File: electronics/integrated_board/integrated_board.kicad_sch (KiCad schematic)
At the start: 69 parts, among them CON1 BARREL_JACK, J1 rot_encoderZ(35,34), J10 pcf8575 IO expander, J11 Switch 1, J13 motor1(15,2,0,4), J15 motor2 (16,17,5,18), J17 motor3 (19,21,22,23), J2 rot_encoderY(25,26), J3 rot_encoderX(14,27), J4 Switch 2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

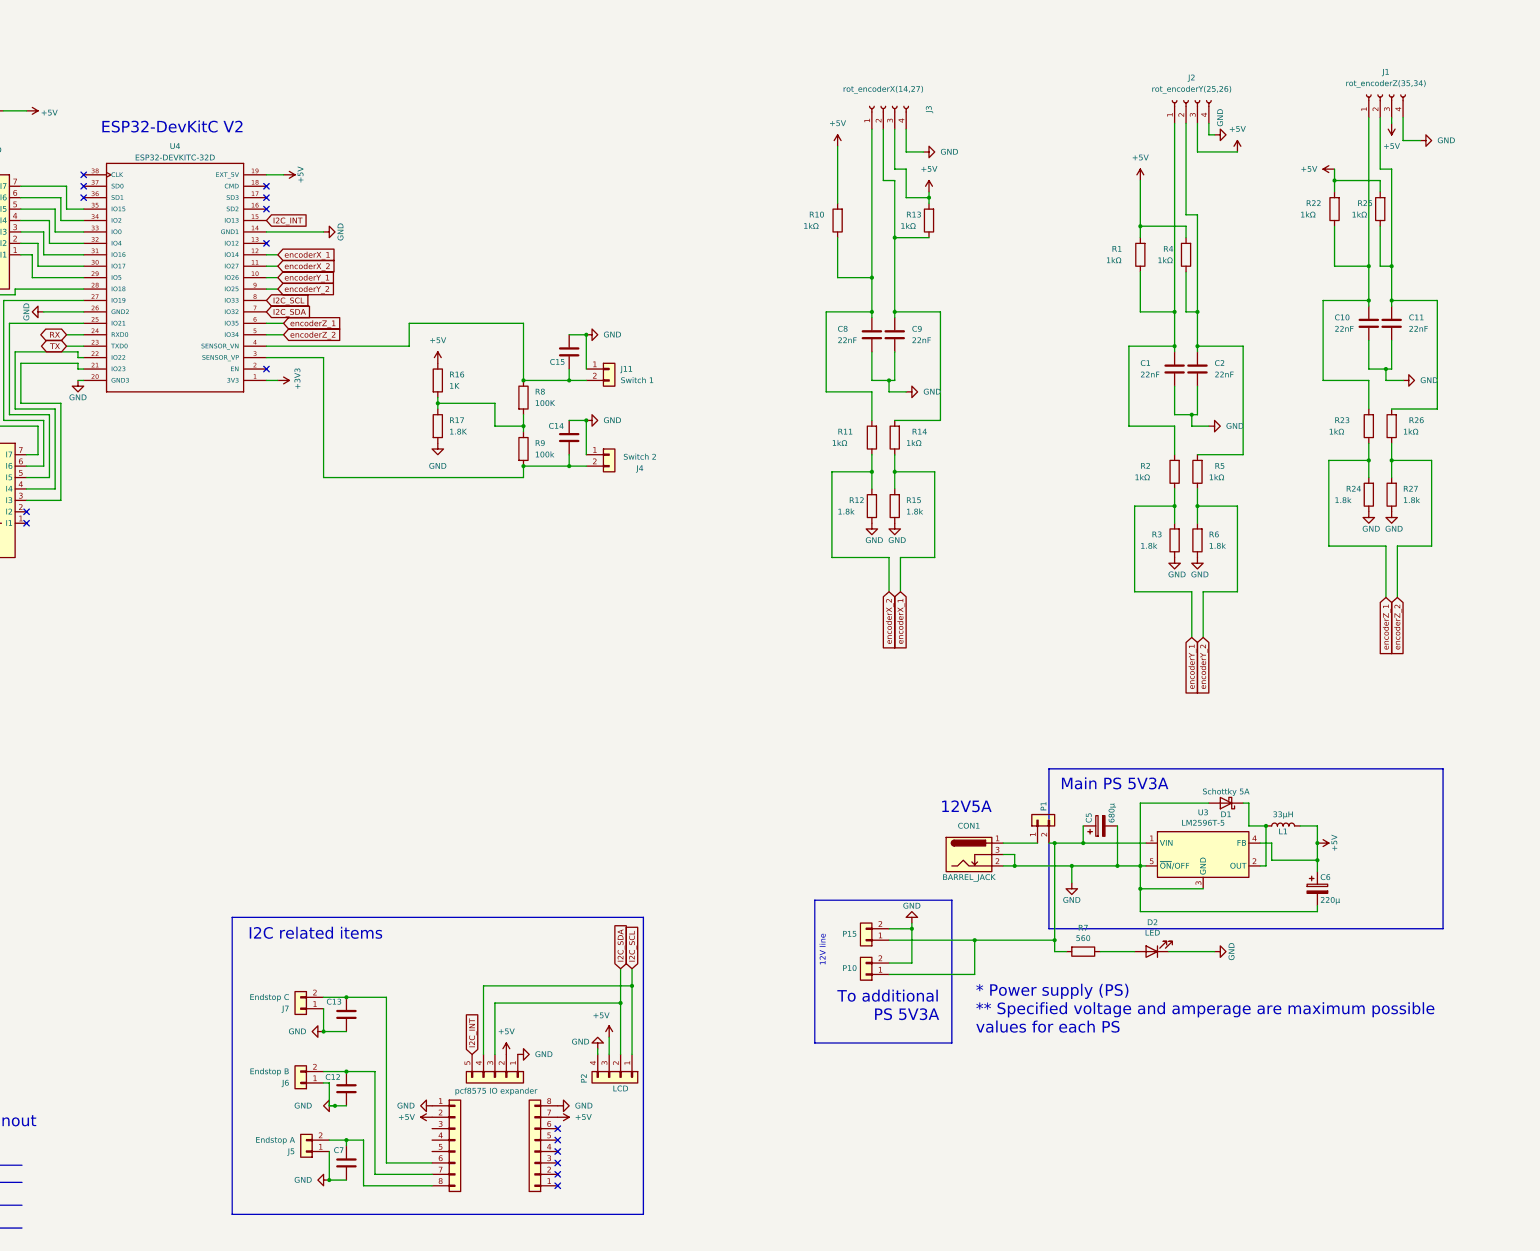
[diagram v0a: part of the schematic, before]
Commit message: Updated integrated PCB
- fixed footprint for pcf8575
- updated footprint for rotary encoder connectors for ease of use
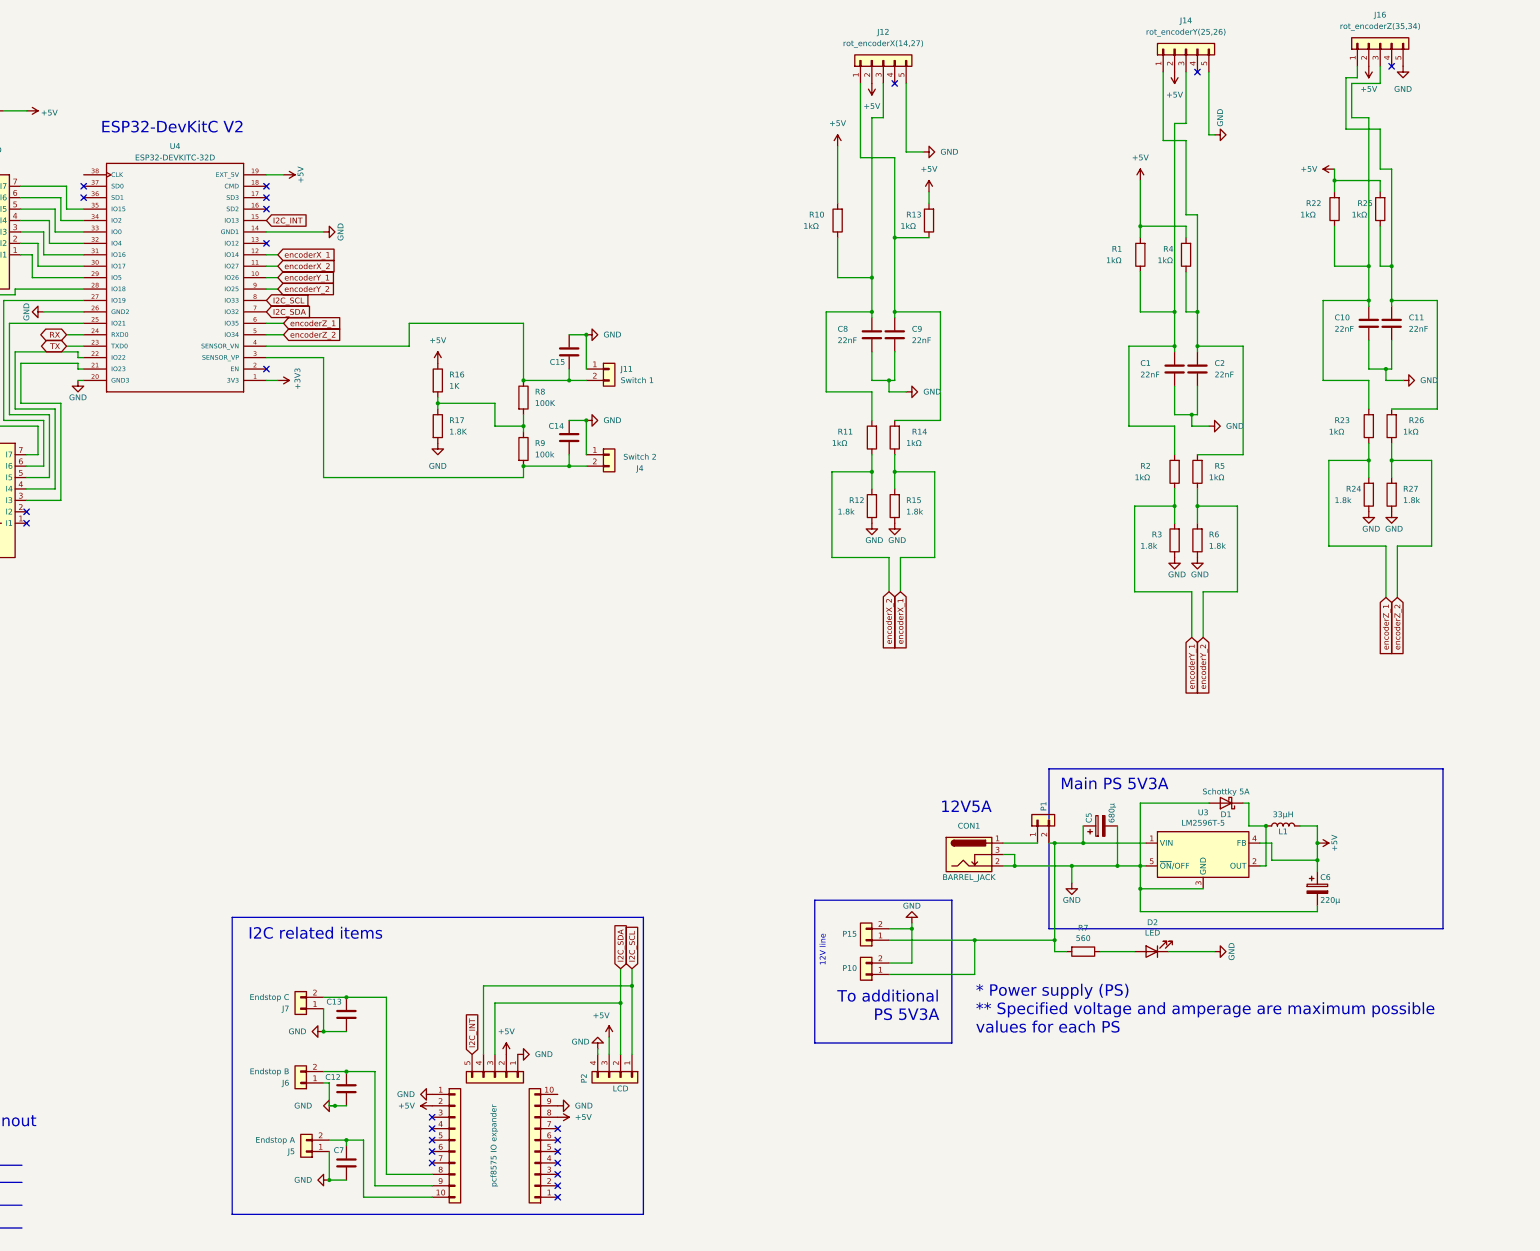
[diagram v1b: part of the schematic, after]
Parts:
- removed J1: rot_encoderZ(35,34), Connector_JST:JST_XH_B4B-XH-A_1x04_P2.50mm_Vertical, symbol Connector:Conn_01x04_Female
- removed J2: rot_encoderY(25,26), Connector_JST:JST_XH_B4B-XH-A_1x04_P2.50mm_Vertical, symbol Connector:Conn_01x04_Female
- removed J3: rot_encoderX(14,27), Connector_JST:JST_XH_B4B-XH-A_1x04_P2.50mm_Vertical, symbol Connector:Conn_01x04_Female
- added J12: rot_encoderX(14,27), Connector_JST:JST_XH_B5B-XH-A_1x05_P2.50mm_Vertical, symbol Connector_Generic:Conn_01x05
- added J14: rot_encoderY(25,26), Connector_JST:JST_XH_B5B-XH-A_1x05_P2.50mm_Vertical, symbol Connector_Generic:Conn_01x05
- added J16: rot_encoderZ(35,34), Connector_JST:JST_XH_B5B-XH-A_1x05_P2.50mm_Vertical, symbol Connector_Generic:Conn_01x05
- J8, J9: footprint Connector_PinHeader_2.54mm:PinHeader_1x08_P2.54mm_Vertical -> Connector_PinHeader_2.54mm:PinHeader_1x10_P2.54mm_Vertical; symbol Connector_Generic:Conn_01x08 -> Connector_Generic:Conn_01x10
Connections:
- net +5V: now also J8.8 (Pin_8), J12.2 (Pin_2), J14.2 (Pin_2), J16.2 (Pin_2); no longer J8.7 (Pin_7)
- net GND: now also J8.9 (Pin_9), J12.5 (Pin_5), J14.5 (Pin_5), J16.5 (Pin_5); no longer J8.8 (Pin_8)
- net at C10.2, R22.1, R23.2: now also J16.3 (Pin_3)
- net at C11.2, R25.1, R26.2: now also J16.1 (Pin_1)
- net at C8.2, R10.1, R11.2: now also J12.3 (Pin_3)
- net at C2.2, R4.1, R5.2: now also J14.1 (Pin_1)
- net at C9.2, R13.1, R14.2: now also J12.1 (Pin_1)
- net at C7.2, J5.2 (Pin_2): now also J9.10 (Pin_10); no longer J9.8 (Pin_8)
- net at C1.2, R1.1, R2.2: now also J14.3 (Pin_3)
- net at C12.2, J6.2 (Pin_2): now also J9.9 (Pin_9); no longer J9.7 (Pin_7)
- net at C13.2, J7.2 (Pin_2): now also J9.8 (Pin_8); no longer J9.6 (Pin_6)
- no-connect marks 18 -> 26

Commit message: Added BNC connectors to board
Intended as receivers of trigger signal for Z-stack
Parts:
- removed P10, P15: Conn_01x02, Connector_JST:JST_XH_B2B-XH-A_1x02_P2.50mm_Vertical, symbol Connector_Generic:Conn_01x02
- added J1, J2: Conn_Coaxial, Connector_Coaxial:BNC_Amphenol_B6252HB-NPP3G-50_Horizontal, symbol Connector:Conn_Coaxial
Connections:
- net GND: now also J1.2 (Ext), J2.2 (Ext)
- net at J8.1 (Pin_1): now also J1.1 (In)
- net at J8.2 (Pin_2): now also J2.1 (In)
- no-connect marks 26 -> 24
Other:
- note removed: "12V line"
- note removed: "To additional PS 5V3A"
